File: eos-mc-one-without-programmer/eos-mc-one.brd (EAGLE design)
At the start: 68.1 x 32.2 mm, 12 parts, among them IC1 ATMEGA328-20P, J1 F-1X04-SIP-100-40, J2 F-1X12-SIP-100-32Y, J3 F-1X12-SIP-100-32Y, Q1 16 MHz

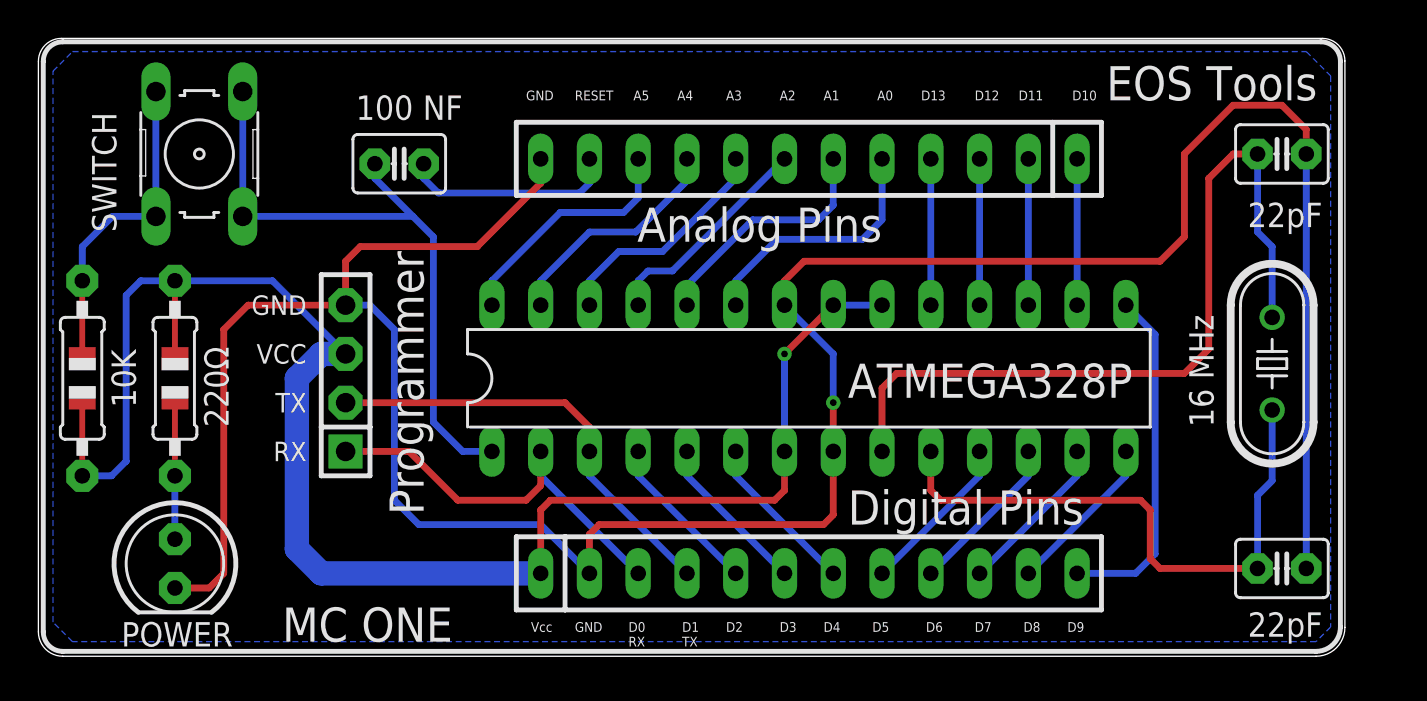
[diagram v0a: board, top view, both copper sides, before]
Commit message: Increased track width
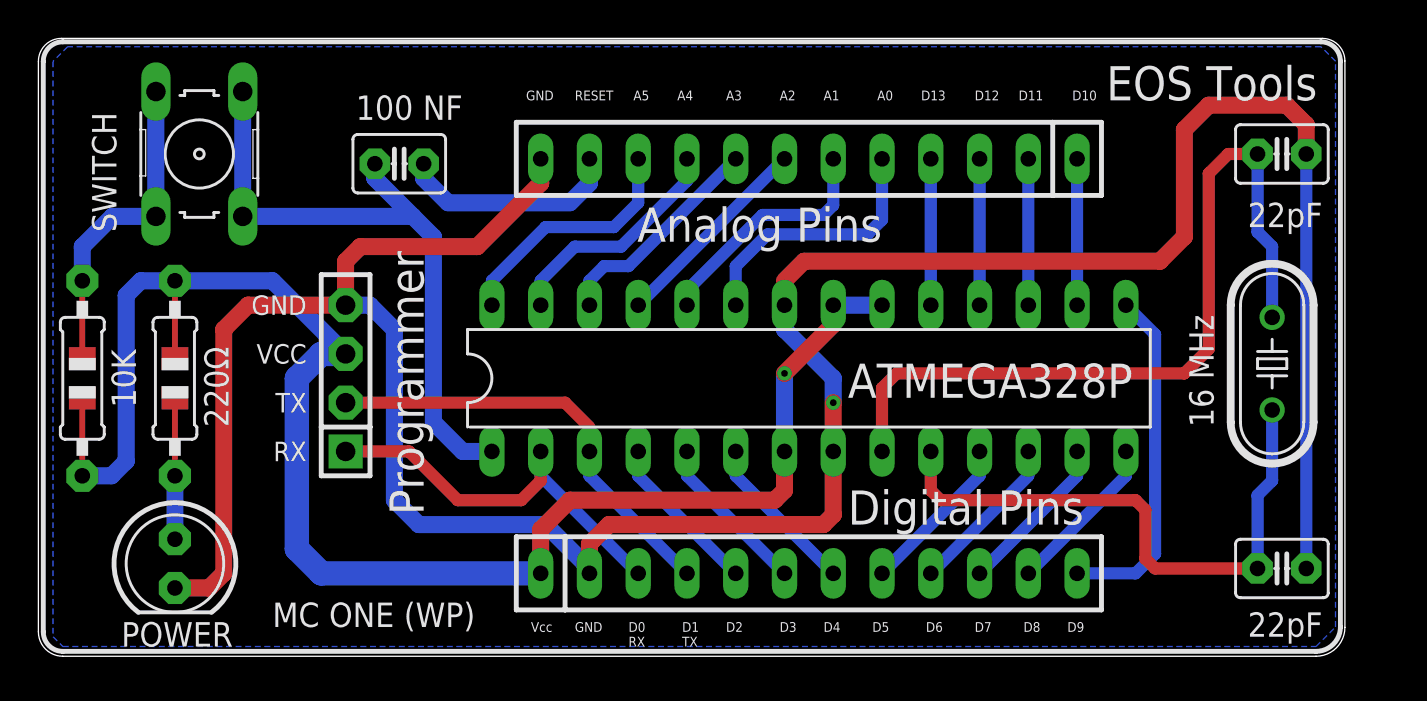
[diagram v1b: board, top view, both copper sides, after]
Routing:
- net N$4: track 146.8 -> 147.5 mm
- net N$22: track 11.5 -> 10.8 mm
- net N$8: track 79.4 -> 78.8 mm
- net N$23: track 12.1 -> 11.5 mm
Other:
- board text added: "MC ONE (WP)"
- board text removed: "MC ONE"

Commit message: Added new code
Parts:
- added C3: 100nF, capacitor-wima:C2.5-3
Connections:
- new net N$28: C3.2, IC1.21
- net N$4: now also C3.1
- net N$8: no longer IC1.21
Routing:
- net N$28: track 0.00 -> 19.5 mm, vias 0 -> 1
- net N$4: track 147.5 -> 150.1 mm
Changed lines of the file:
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@@
 <attribute name="POPULARITY" value="38" x="20.574" y="26.416" size="1.778" layer="27" rot="R180" display="off"/>
+</element>
+<element name="C3" library="capacitor-wima" library_urn="urn:adsk.eagle:library:116" package="C2.5-3" package3d_urn="urn:adsk.eagle:package:5436/1" value="100nF" x="59.436" y="25.654" smashed="yes" rot="R270">
+<attribute name="NAME" x="61.214" y="27.305" size="1.27" layer="25" ratio="10" rot="R270"/>
+<attribute name="POPULARITY" value="38" x="59.436" y="25.654" size="1.778" layer="27" rot="R270" display="off"/>
+<attribute name="VALUE" x="56.896" y="21.209" size="1.27" layer="27" ratio="10"/>
 </element>
 </elements>
@@
 <vertex x="3.302" y="32.512"/>
 </polygon>
+<contactref element="C3" pad="1"/>
+<wire x1="59.436" y1="26.924" x2="60.706" y2="28.194" width="0.889" layer="1"/>
+<wire x1="60.706" y1="28.194" x2="61.468" y2="28.194" width="0.889" layer="1"/>
 </signal>
 <signal name="N$3">
@@
 </signal>
 <signal name="N$8">
-<contactref element="IC1" pad="21"/>
 <contactref element="IC1" pad="20"/>
 <contactref element="R5" pad="1"/>
@@
 <via x="40.64" y="15.494" extent="1-16" drill="0.35"/>
 <wire x1="40.64" y1="11.43" x2="40.64" y2="15.494" width="0.889" layer="16"/>
-<wire x1="43.18" y1="18.034" x2="43.18" y2="19.05" width="0.889" layer="1"/>
-<wire x1="43.18" y1="18.034" x2="40.64" y2="15.494" width="0.889" layer="1"/>
-<wire x1="43.18" y1="19.05" x2="45.72" y2="19.05" width="0.889" layer="16"/>
 <wire x1="27.94" y1="5.08" x2="27.94" y2="7.366" width="0.889" layer="1"/>
 <wire x1="27.94" y1="7.366" x2="29.464" y2="8.89" width="0.889" layer="1"/>
@@
 <wire x1="5.588" y1="10.16" x2="4.064" y2="10.16" width="0.889" layer="16"/>
 <wire x1="8.89" y1="20.32" x2="7.112" y2="20.32" width="0.889" layer="16"/>
+<wire x1="40.64" y1="15.494" x2="41.656" y2="16.51" width="0.889" layer="1"/>
+<wire x1="41.656" y1="16.51" x2="44.704" y2="16.51" width="0.889" layer="1"/>
+<wire x1="44.704" y1="16.51" x2="45.72" y2="17.526" width="0.889" layer="1"/>
+<wire x1="45.72" y1="17.526" x2="45.72" y2="19.05" width="0.889" layer="1"/>
 </signal>
 <signal name="N$5">
@@
 <wire x1="21.844" y1="26.416" x2="21.844" y2="25.654" width="0.889" layer="16"/>
 </signal>
+<signal name="N$28">
+<contactref element="IC1" pad="21"/>
+<contactref element="C3" pad="2"/>
+<wire x1="59.436" y1="24.384" x2="59.436" y2="23.368" width="0.6096" layer="1"/>
+<wire x1="59.436" y1="23.368" x2="58.674" y2="22.606" width="0.6096" layer="1"/>
+<wire x1="58.674" y1="22.606" x2="47.244" y2="22.606" width="0.6096" layer="1"/>
+<via x="47.244" y="22.606" extent="1-16" drill="0.35"/>
+<wire x1="43.18" y1="19.05" x2="43.18" y2="19.812" width="0.6096" layer="16"/>
+<wire x1="45.974" y1="22.606" x2="47.244" y2="22.606" width="0.6096" layer="16"/>
+<wire x1="43.18" y1="19.812" x2="45.974" y2="22.606" width="0.6096" layer="16"/>
+</signal>
 </signals>

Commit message: Added new design
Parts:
- moved C3 0.57 mm to (59.2, 26.2)
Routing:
- net N$20: track 13.8 -> 13.2 mm
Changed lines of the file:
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@@
 <attribute name="POPULARITY" value="38" x="20.574" y="26.416" size="1.778" layer="27" rot="R180" display="off"/>
 </element>
-<element name="C3" library="capacitor-wima" library_urn="urn:adsk.eagle:library:116" package="C2.5-3" package3d_urn="urn:adsk.eagle:package:5436/1" value="100nF" x="59.436" y="25.654" smashed="yes" rot="R270">
-<attribute name="NAME" x="61.214" y="27.305" size="1.27" layer="25" ratio="10" rot="R270"/>
-<attribute name="POPULARITY" value="38" x="59.436" y="25.654" size="1.778" layer="27" rot="R270" display="off"/>
-<attribute name="VALUE" x="56.896" y="21.209" size="1.27" layer="27" ratio="10"/>
+<element name="C3" library="capacitor-wima" library_urn="urn:adsk.eagle:library:116" package="C2.5-3" package3d_urn="urn:adsk.eagle:package:5436/1" value="100nF" x="59.182" y="26.162" smashed="yes" rot="R270">
+<attribute name="POPULARITY" value="38" x="59.182" y="26.162" size="1.778" layer="27" rot="R270" display="off"/>
+<attribute name="VALUE" x="56.642" y="21.717" size="1.27" layer="27" ratio="10"/>
 </element>
 </elements>
@@
 </polygon>
 <contactref element="C3" pad="1"/>
-<wire x1="59.436" y1="26.924" x2="60.706" y2="28.194" width="0.889" layer="1"/>
-<wire x1="60.706" y1="28.194" x2="61.468" y2="28.194" width="0.889" layer="1"/>
+<wire x1="59.182" y1="27.432" x2="59.944" y2="28.194" width="0.889" layer="1"/>
+<wire x1="59.944" y1="28.194" x2="61.468" y2="28.194" width="0.889" layer="1"/>
 </signal>
 <signal name="N$3">
@@
 <wire x1="38.1" y1="19.05" x2="38.1" y2="21.082" width="0.635" layer="16"/>
 <wire x1="39.751" y1="22.733" x2="38.1" y2="21.082" width="0.635" layer="16"/>
-<wire x1="39.751" y1="22.733" x2="44.958" y2="22.733" width="0.635" layer="16"/>
-<wire x1="44.958" y1="22.733" x2="45.72" y2="23.495" width="0.635" layer="16"/>
-<wire x1="45.72" y1="23.495" x2="45.72" y2="26.67" width="0.635" layer="16"/>
+<wire x1="39.751" y1="22.733" x2="43.942" y2="22.733" width="0.635" layer="16"/>
+<wire x1="43.942" y1="22.733" x2="45.72" y2="24.511" width="0.635" layer="16"/>
+<wire x1="45.72" y1="24.511" x2="45.72" y2="26.67" width="0.635" layer="16"/>
 </signal>
 <signal name="N$21">
@@
 <contactref element="IC1" pad="21"/>
 <contactref element="C3" pad="2"/>
-<wire x1="59.436" y1="24.384" x2="59.436" y2="23.368" width="0.6096" layer="1"/>
-<wire x1="59.436" y1="23.368" x2="58.674" y2="22.606" width="0.6096" layer="1"/>
+<wire x1="59.182" y1="24.892" x2="59.182" y2="23.114" width="0.6096" layer="1"/>
+<wire x1="59.182" y1="23.114" x2="58.674" y2="22.606" width="0.6096" layer="1"/>
 <wire x1="58.674" y1="22.606" x2="47.244" y2="22.606" width="0.6096" layer="1"/>
 <via x="47.244" y="22.606" extent="1-16" drill="0.35"/>
